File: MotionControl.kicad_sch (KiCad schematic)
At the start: 25 parts, among them J2 Conn_ARM_JTAG_SWD_10, Q1 2N7002, SW1 SW_Push, U1 ATSAMD21J18A-A, U7 TC4427, Y1 32.768kHz

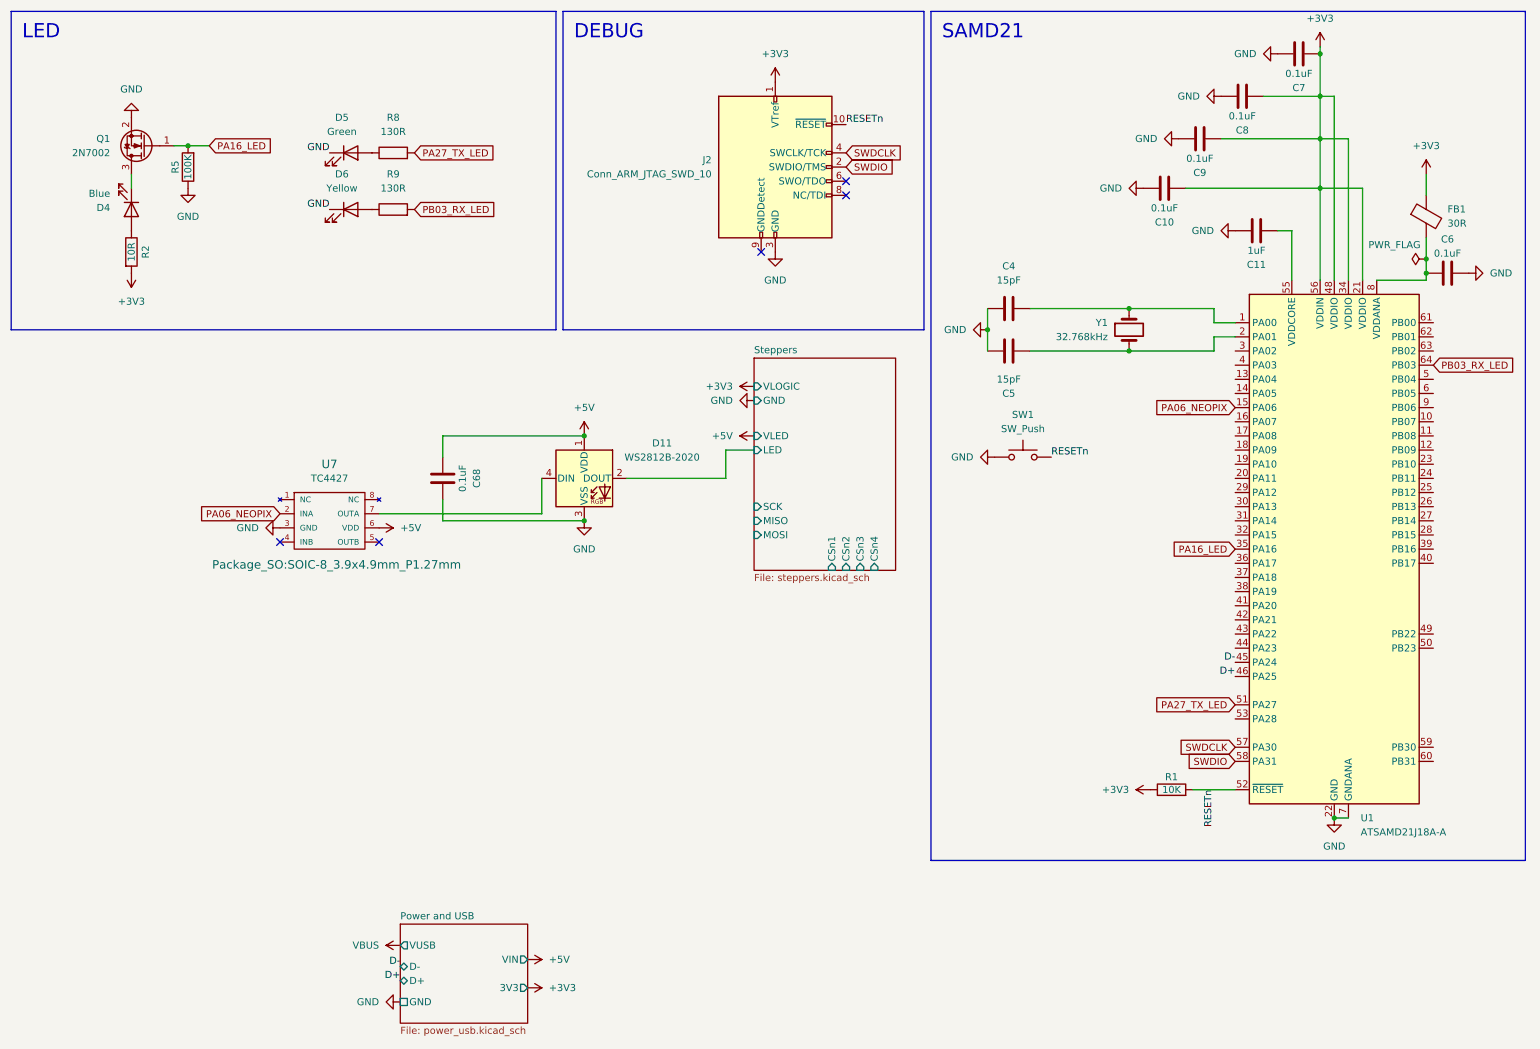
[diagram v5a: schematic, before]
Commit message: Begin spi routing
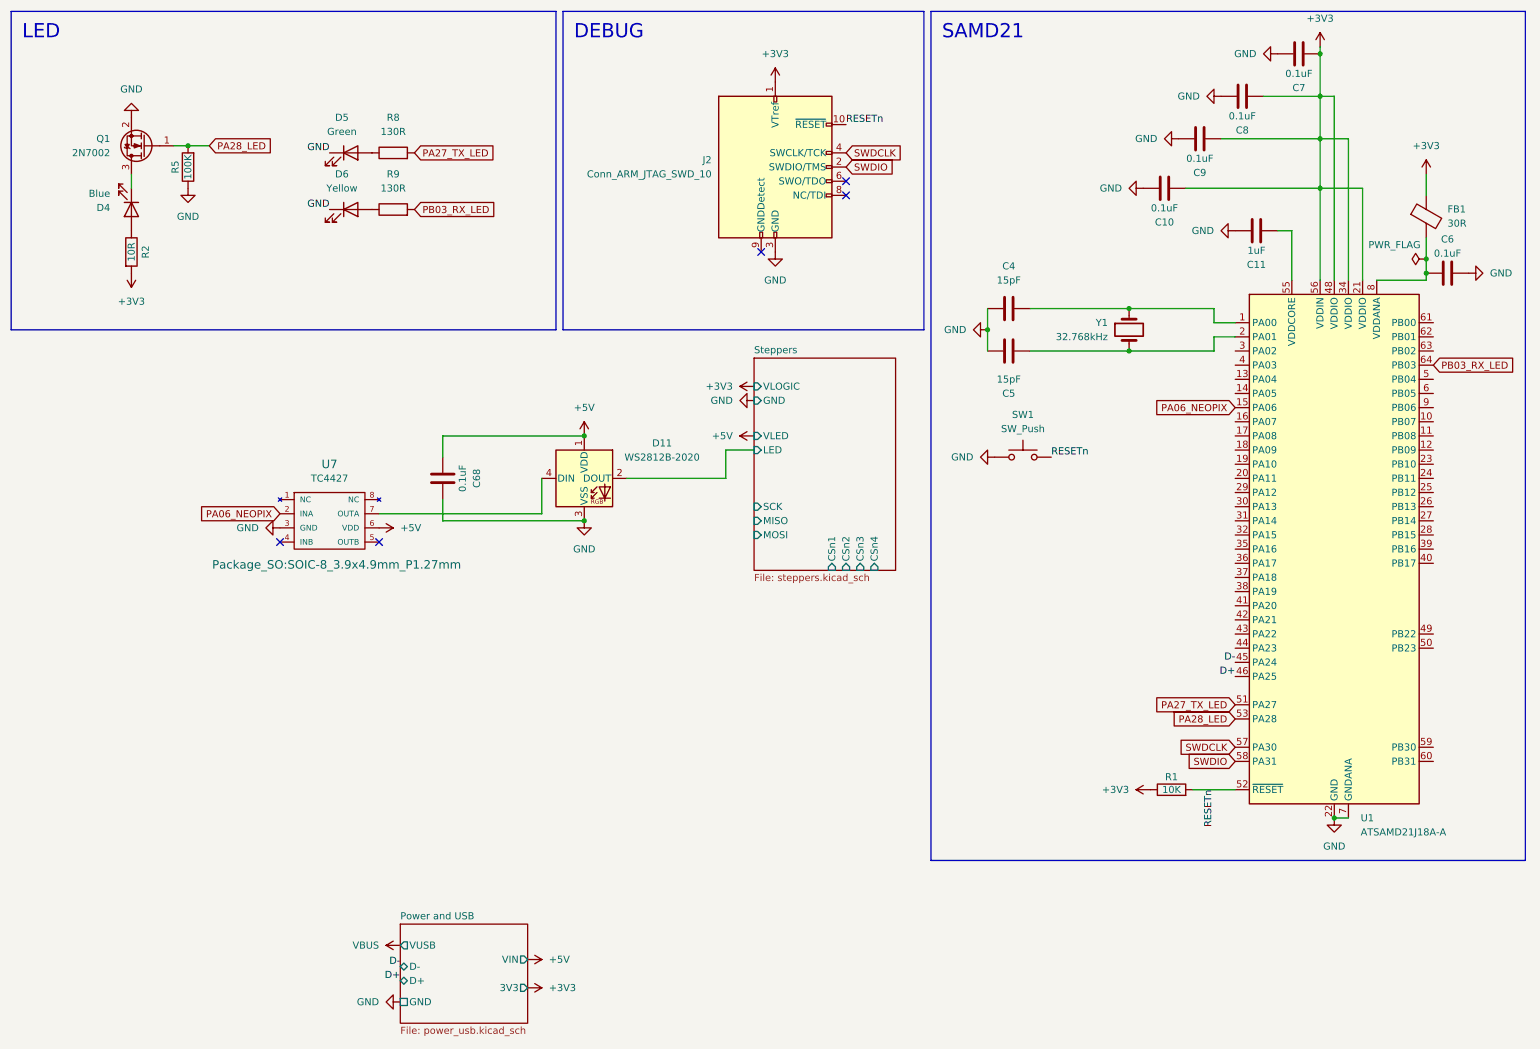
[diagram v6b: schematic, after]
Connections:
- net PA28_LED: now reaches U1.53 (PA28)
- net PA28_LED: now also Q1.1 (G), R5.2
- removed net PA16_LED: Q1.1 (G), R5.2, U1.35 (PA16)
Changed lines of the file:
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@@
+		)
+	)
+	(global_label "PA28_LED"
+		(shape input)
+		(at 232.41 139.7 180)
+		(fields_autoplaced yes)
+		(effects
+			(font
+				(size 1.27 1.27)
+			)
+			(justify right)
+		)
+		(property "Intersheetrefs" "${INTERSHEET_REFS}"
+			(at 220.2325 139.7 0)
+			(effects
+				(font
+					(size 1.27 1.27)
+				)
+				(justify right)
+				(hide yes)
+			)
 		)
 	)
@@
 		)
 	)
-	(global_label "PA16_LED"
-		(shape input)
-		(at 232.41 109.22 180)
-		(fields_autoplaced yes)
-		(effects
-			(font
-				(size 1.27 1.27)
-			)
-			(justify right)
-		)
-		(property "Intersheetrefs" "${INTERSHEET_REFS}"
-			(at 220.2325 109.22 0)
-			(effects
-				(font
-					(size 1.27 1.27)
-				)
-				(justify right)
-				(hide yes)
-			)
-		)
-	)
 	(global_label "SWDCLK"
 		(shape input)
@@
 		(property "Intersheetrefs" "${INTERSHEET_REFS}"
 			(at 173.0442 38.1 0)
-			(effects
-				(font
-					(size 1.27 1.27)
-				)
-				(justify left)
-				(hide yes)
-			)
-		)
-	)
-	(global_label "PA16_LED"
-		(shape input)
-		(at 48.26 36.83 0)
-		(fields_autoplaced yes)
-		(effects
-			(font
-				(size 1.27 1.27)
-			)
-			(justify left)
-		)
-		(property "Intersheetrefs" "${INTERSHEET_REFS}"
-			(at 60.4375 36.83 0)
 			(effects
 				(font
@@
 			(effects
 				(font
+					(size 1.27 1.27)
+				)
+				(justify left)
+				(hide yes)
+			)
+		)
+	)
+	(global_label "PA28_LED"
+		(shape input)
+		(at 48.26 36.83 0)
+		(fields_autoplaced yes)
+		(effects
+			(font
+				(size 1.27 1.27)
+			)
+			(justify left)
+		)
+		(property "Intersheetrefs" "${INTERSHEET_REFS}"
+			(at 60.4375 36.83 0)
+			(effects
+				(font

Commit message: Route tmc spi busses, cs
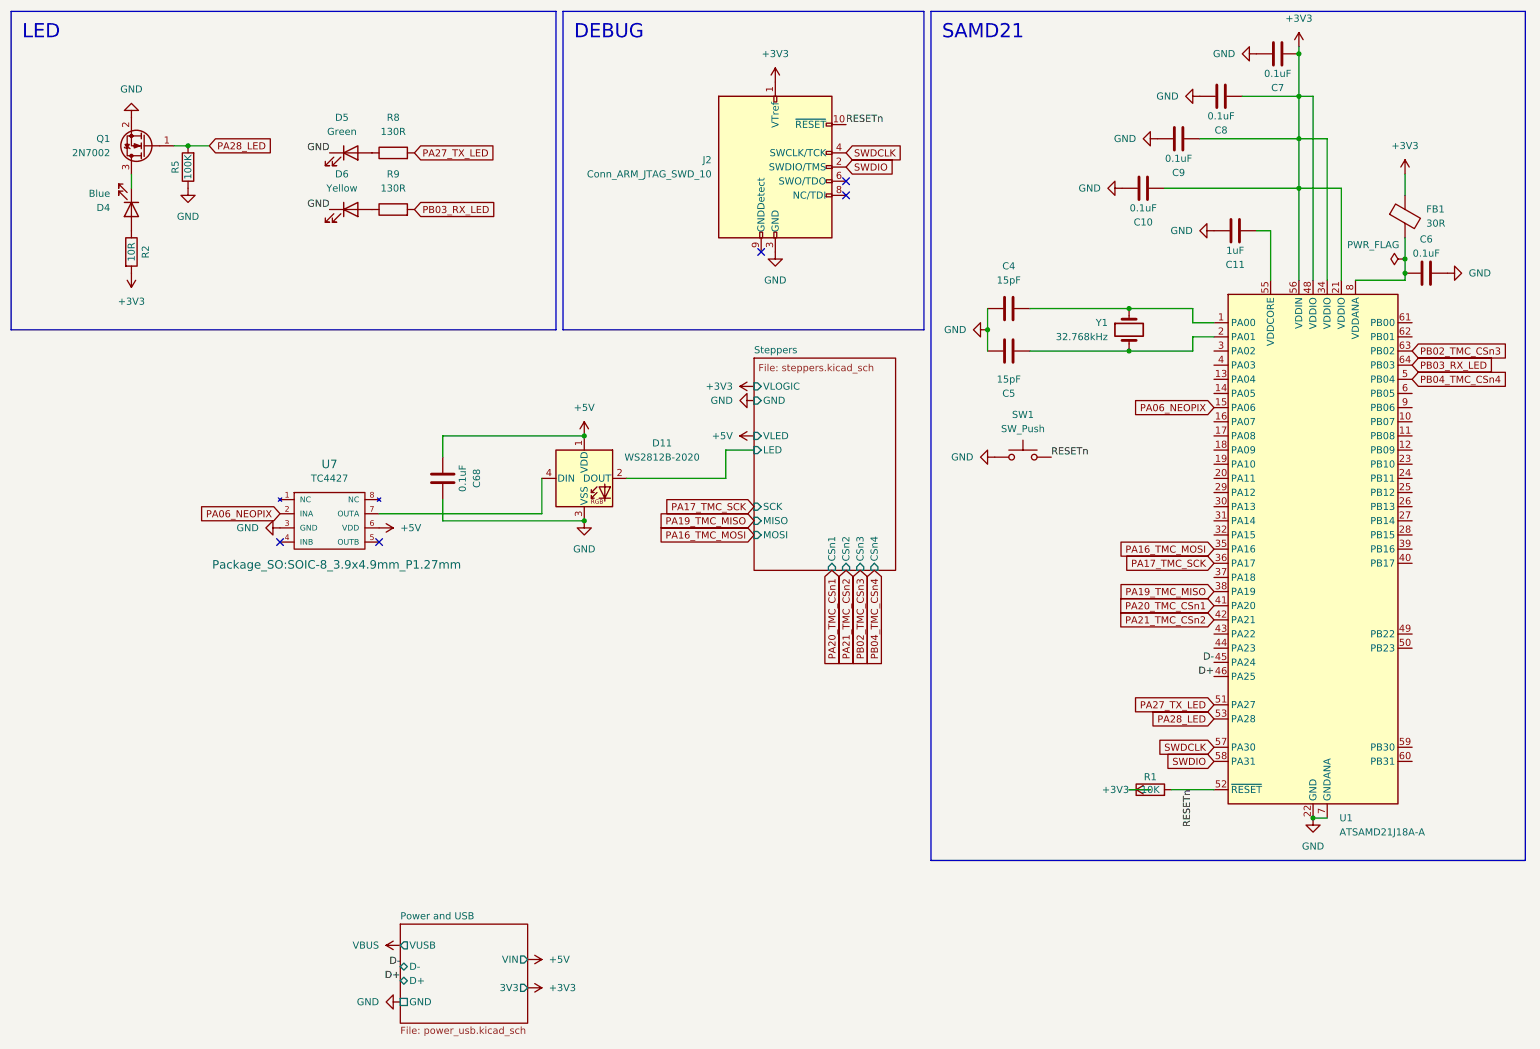
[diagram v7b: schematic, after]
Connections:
- net PA16_TMC_MOSI: now reaches U1.35 (PA16)
- net PA17_TMC_SCK: now reaches U1.36 (PA17)
- net PA19_TMC_MISO: now reaches U1.38 (PA19)
- net PA20_TMC_CSn1: now reaches U1.41 (PA20)
- net PA21_TMC_CSn2: now reaches U1.42 (PA21)
- net PB04_TMC_CSn4: now reaches U1.5 (PB04)
- net PB02_TMC_CSn3: now reaches U1.63 (PB02)
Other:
- moved on the sheet: C10, C11, C6, C7, C8, C9, FB1, R1, U1

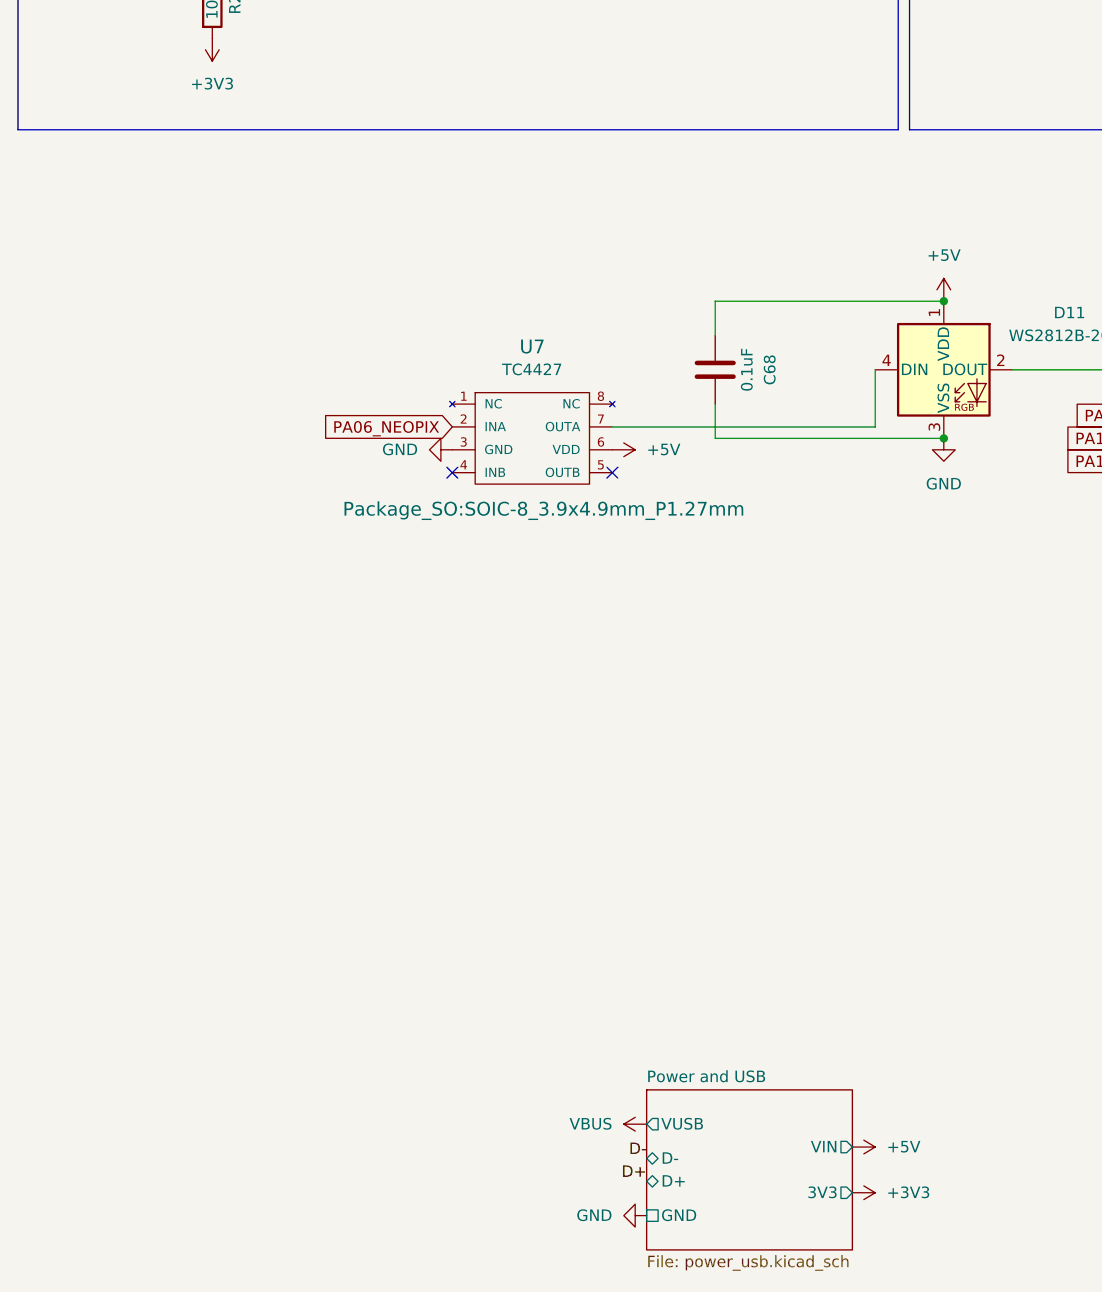
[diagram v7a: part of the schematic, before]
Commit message: Begin addition of mag sensor conns
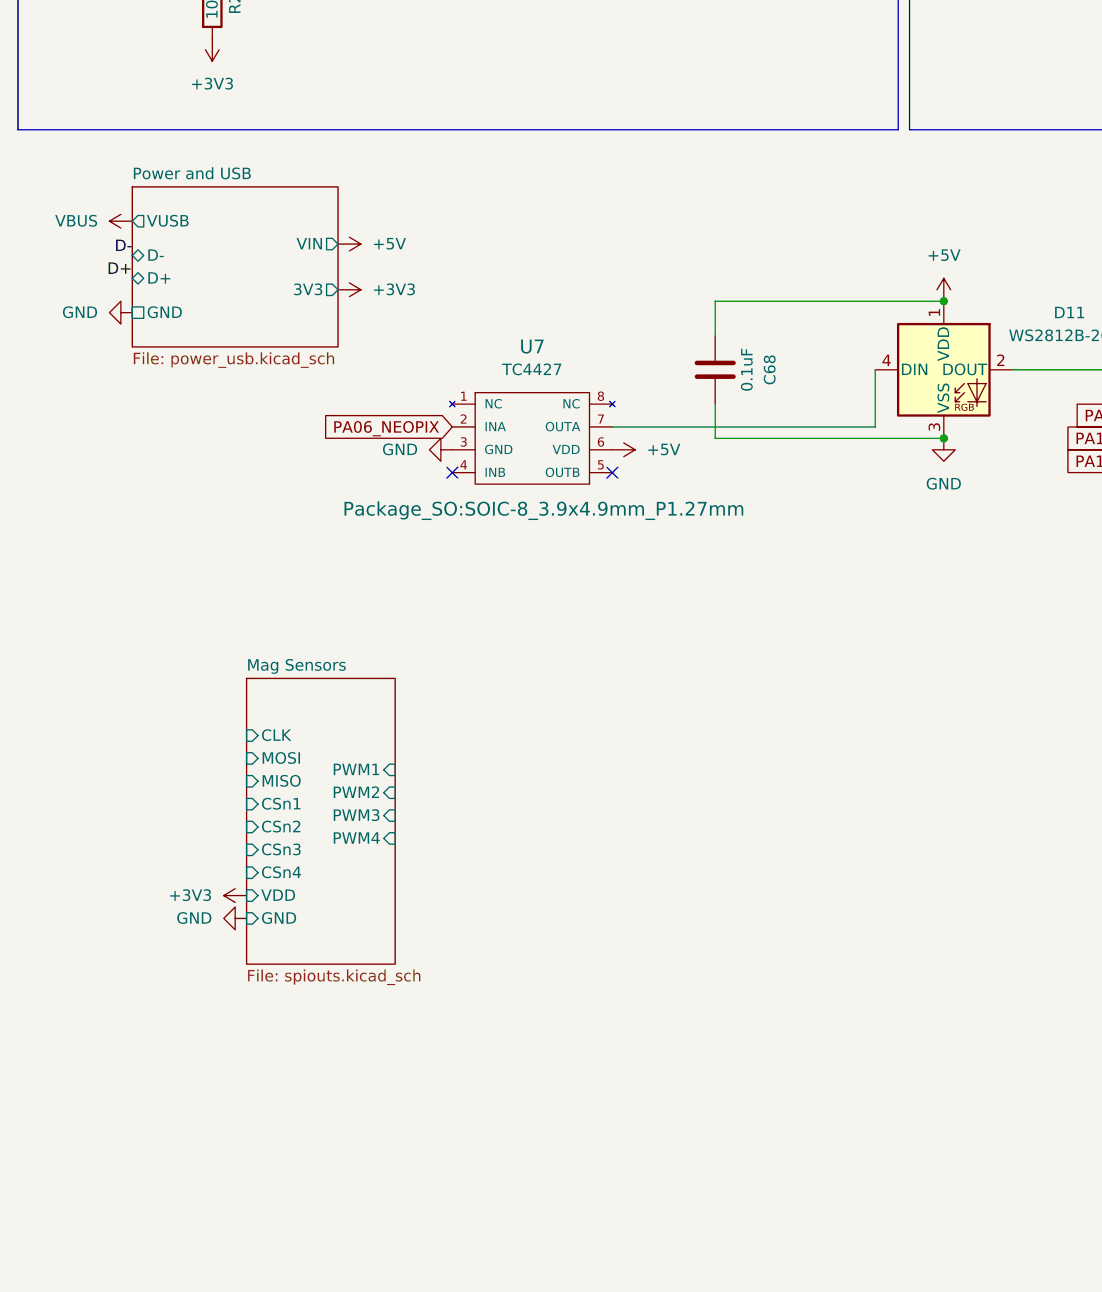
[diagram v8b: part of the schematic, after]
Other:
- added sheet Mag Sensors (spiouts.kicad_sch)
